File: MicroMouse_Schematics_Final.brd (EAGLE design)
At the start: 227 x 80 mm, 63 parts

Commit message: Add files via upload
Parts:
- added E$1: (no value), MOUSE_OUTLINE_2WHEEL:MOUSE_OUTLINE_2WHEEL
- moved C4 394.5 mm to (123.2, 33.0), turned to 180 degrees
- moved B2 390.8 mm to (142.2, 54.6)
- moved B1 386.4 mm to (142.2, 48.3)
- moved C5 383.9 mm to (123.2, 59.7), turned to 180 degrees
- moved C7 374.4 mm to (83.8, 27.9), turned to 180 degrees
- moved C6 365.3 mm to (76.2, 27.9), turned to 90 degrees
- moved C1 354.4 mm to (144.8, 39.4), turned to 180 degrees
- moved POLOLU_SWITCH 352.9 mm to (144.8, 31.8), turned to 90 degrees
- moved BAT_JST-PH 352.4 mm to (144.8, 21.6), turned to 90 degrees
- moved C2000 344.7 mm to (76.2, 47.0), turned to 90 degrees
- moved LED_PWR 336.0 mm to (74.9, 17.8), turned to 90 degrees
- moved C2 331.1 mm to (127.0, 63.5), turned to 90 degrees
- moved R18 330.6 mm to (133.3, 21.6), turned to 270 degrees
- moved R19 329.6 mm to (133.3, 26.7), turned to 90 degrees
- moved LED1 321.0 mm to (64.8, 34.3), turned to 180 degrees
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
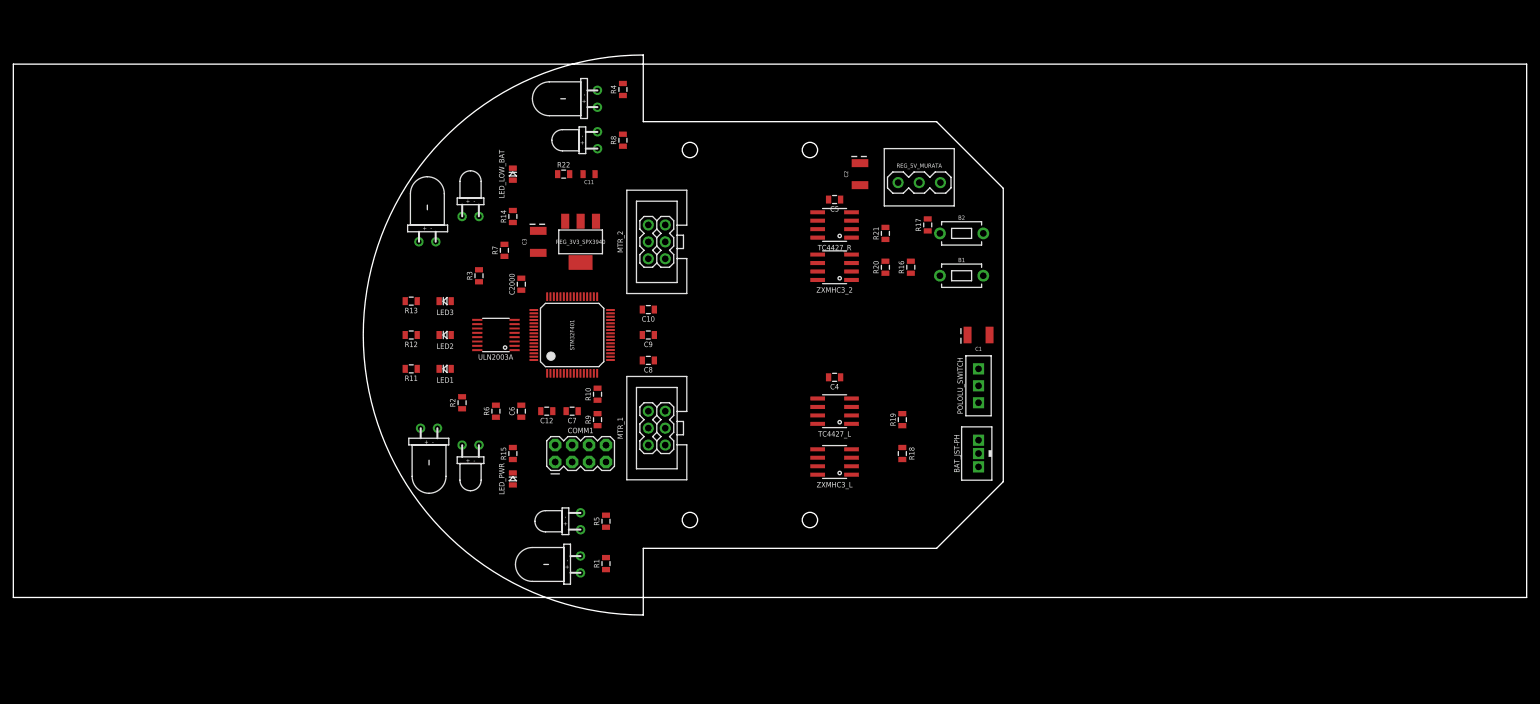
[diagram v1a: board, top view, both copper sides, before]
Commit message: GND Pin & Autoroute
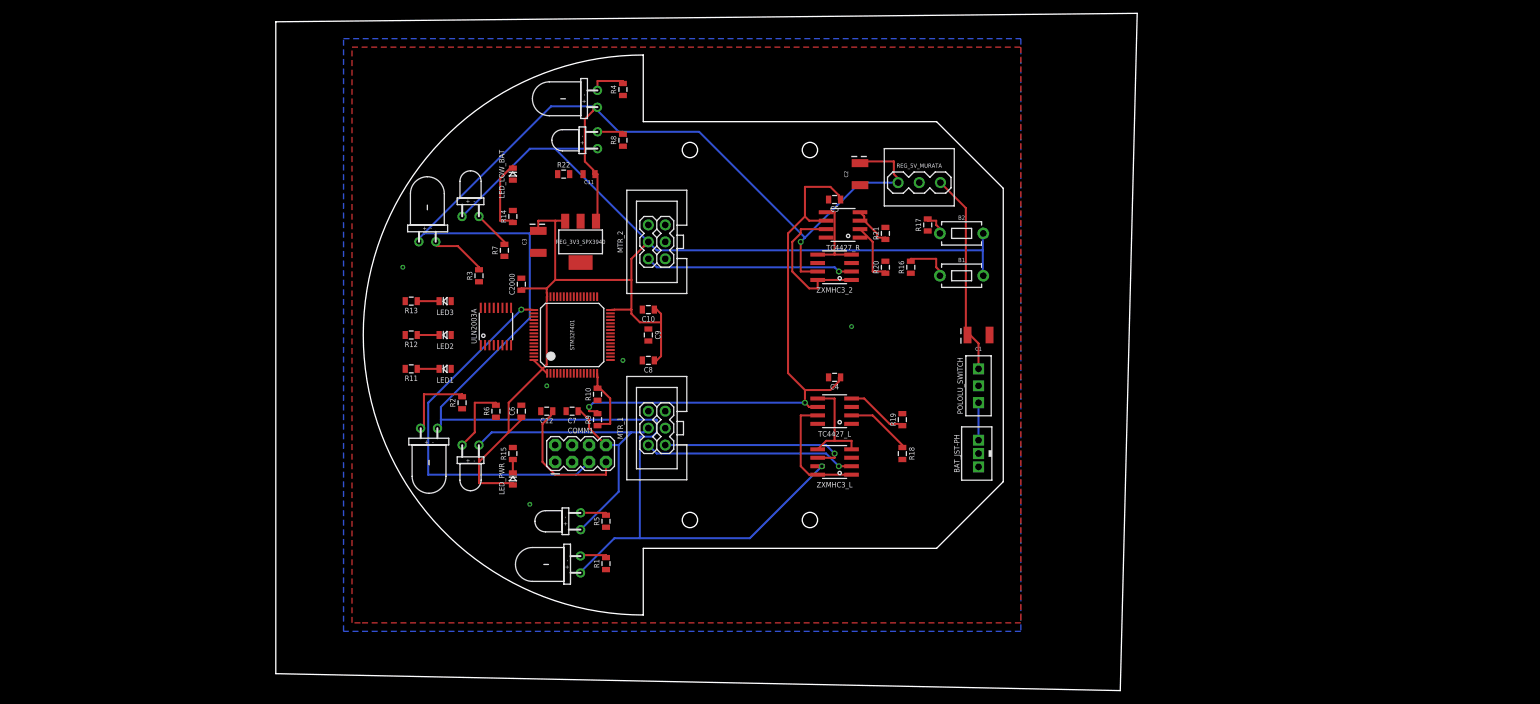
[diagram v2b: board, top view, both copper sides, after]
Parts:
- moved ULN2003A 1.27 mm to (72.4, 40.6), turned to 90 degrees
- moved TC4427_R 1.27 mm to (124.5, 55.9)
- turned C9 to 270 degrees
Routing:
- net +5V: track 0.00 -> 275.7 mm, vias 0 -> 2
- net +3V3: track 0.00 -> 262.8 mm
- net VBAT: track 0.00 -> 88.0 mm, vias 0 -> 2
- net SWCLK: track 0.00 -> 57.3 mm, vias 0 -> 1
- net LMTR+: track 0.00 -> 31.8 mm, vias 0 -> 1
- net RMTR+: track 0.00 -> 31.3 mm, vias 0 -> 1
- net N$3: track 0.00 -> 30.7 mm
- net LMTR-: track 0.00 -> 29.1 mm, vias 0 -> 1
- net N$21: track 0.00 -> 21.9 mm
- net NRST: track 0.00 -> 20.6 mm
- net N$12: track 0.00 -> 18.3 mm
- net N$15: track 0.00 -> 15.8 mm
- net N$25: track 0.00 -> 12.7 mm
- net N$16: track 0.00 -> 11.7 mm
- net N$8: track 0.00 -> 11.6 mm
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- added copper zone on layer 1, net GND
- added copper zone on layer 16, net GND
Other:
- board size 227 x 80 mm -> 129.2 x 101.6 mm

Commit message: Add files via upload
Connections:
- new net S$1: R3.2
- new net S$2: C8.1
- net +3V3: no longer C8.1
- net N$17: no longer R3.2
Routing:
- net GND: track 0.00 -> 297.5 mm
- net B0: track 7.06 -> 99.2 mm
- net N$7: track 0.00 -> 77.0 mm
- net LED1: track 0.00 -> 55.6 mm
- net N$13: track 0.00 -> 41.7 mm
- net N$11: track 0.00 -> 17.1 mm
- net N$9: track 0.00 -> 16.6 mm
- net EM_LD: track 0.00 -> 9.10 mm
- net N$17: track 8.80 -> 0.76 mm
- net GND4: track 0.00 -> 6.84 mm, vias 0 -> 1
- net +3V3: track 262.8 -> 256.5 mm

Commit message: Rough Draft 1
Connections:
- removed net S$1: R3.2
- removed net S$2: C8.1
- net +3V3: now also C8.1
- net N$17: now also R3.2
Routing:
- net LPWM_B: track 9.46 -> 165.2 mm, vias 0 -> 10
- net RENC_B: track 0.00 -> 153.1 mm, vias 0 -> 10
- net TX: track 0.00 -> 145.7 mm, vias 0 -> 9
- net RX: track 0.00 -> 137.6 mm, vias 0 -> 5
- net GND: track 297.5 -> 426.3 mm, vias 2 -> 29
- net LED2: track 0.00 -> 96.1 mm, vias 0 -> 6
- net LPWM_A: track 9.83 -> 93.2 mm, vias 0 -> 4
- net RPWM_B: track 6.40 -> 77.6 mm, vias 0 -> 2
- net RPWM_A: track 9.31 -> 77.9 mm, vias 0 -> 2
- net B1: track 3.78 -> 64.5 mm, vias 0 -> 2
- net RE_RD: track 5.76 -> 58.1 mm, vias 0 -> 6
- net RE_RF: track 4.18 -> 46.0 mm, vias 0 -> 2
- net RENC_A: track 0.00 -> 39.7 mm, vias 0 -> 5
- net SWDIO: track 0.00 -> 38.1 mm, vias 0 -> 6
- net N$32: track 0.00 -> 36.5 mm
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
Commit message: Final Board
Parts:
- moved R11 4.06 mm to (55.6, 34.3)
- moved R12 4.06 mm to (55.6, 39.4)
- moved R13 4.06 mm to (55.6, 44.5)
- moved LED1 2.03 mm to (62.7, 34.3)
- moved LED2 1.52 mm to (63.2, 39.4)
- moved LED3 1.52 mm to (63.2, 44.5)
- moved ULN2003A 1.27 mm to (72.4, 39.4), turned to 180 degrees
- moved TC4427_R 1.27 mm to (123.2, 55.9)
- moved C10 0.51 mm to (95.8, 43.2)
- moved R22 0.51 mm to (82.0, 63.5)
- turned C9 to 180 degrees
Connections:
- new net S$1: C10.2, C11.2, C12.2, C2000.2, C3.C, C6.2, C7.2, COMM1.3, COMM1.6, MTR_2.ENC_GND, R10.1, R11.2, R12.2, R13.2, R14.2, R15.2, R22.2, R5.1, R6.1, R7.1, R8.1, REG_3V3_SPX3940.GND, REG_3V3_SPX3940.GND2, STM32F401.PB2, STM32F401.VSSA, STM32F401.VSS_1, ULN2003A.GND
- net GND: no longer C10.2, C11.2, C12.2, C2000.2, C3.C, C6.2, C7.2, COMM1.3, COMM1.6, MTR_2.ENC_GND, R10.1, R11.2, R12.2, R13.2, R14.2, R15.2, R22.2, R5.1, R6.1, R7.1, R8.1, REG_3V3_SPX3940.GND, REG_3V3_SPX3940.GND2, STM32F401.PB2, STM32F401.VSSA, STM32F401.VSS_1, ULN2003A.GND
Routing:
- net S$1: track 0.00 -> 268.1 mm, vias 0 -> 19
- net GND: track 426.3 -> 211.2 mm, vias 29 -> 14
- net TX: track 145.7 -> 46.5 mm, vias 9 -> 2
- net RENC_B: track 153.1 -> 70.4 mm, vias 10 -> 4
- net RPWM_B: track 77.6 -> 133.4 mm, vias 2 -> 8
- net LMTR+: track 31.8 -> 79.3 mm, vias 1 -> 4
- net RE_RF: track 46.0 -> 86.6 mm
- net N$32: track 36.5 -> 72.9 mm, vias 0 -> 4
- net RE_LF: track 4.18 -> 31.2 mm, vias 0 -> 1
- net VBAT: track 88.0 -> 114.1 mm, vias 2 -> 11
- net +5V: track 275.7 -> 249.8 mm, vias 2 -> 8
- net LMTR-: track 29.1 -> 54.6 mm, vias 1 -> 2
- net RENC_A: track 39.7 -> 62.9 mm, vias 5 -> 4
- net RMTR+: track 31.3 -> 53.1 mm, vias 1 -> 4
- net RPWM_A: track 77.9 -> 97.4 mm, vias 2 -> 7
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- removed copper zone on layer 1, net GND
- removed copper zone on layer 16, net GND
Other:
- board size 129.2 x 101.6 mm -> 227 x 80 mm

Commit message: Add files via upload
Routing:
- net RPWM_A: track 97.4 -> 137.1 mm, vias 7 -> 8
- net EM_LF: track 16.8 -> 38.4 mm, vias 0 -> 4
- net S$1: track 268.1 -> 278.5 mm, vias 19 -> 20
- net VBAT: track 114.1 -> 120.0 mm
- net RE_RF: track 86.6 -> 90.5 mm
- net TX: track 46.5 -> 48.7 mm
- net +3V3: track 302.1 -> 300.1 mm
- net RPWM_B: track 133.4 -> 135.3 mm
- net +5V: track 249.8 -> 251.1 mm, vias 8 -> 9
- net RENC_B: track 70.4 -> 71.6 mm
- net SWDIO: track 41.5 -> 42.7 mm
- net GND: track 211.2 -> 212.0 mm, vias 14 -> 15
